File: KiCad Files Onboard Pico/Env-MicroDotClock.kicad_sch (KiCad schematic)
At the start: 60 parts, among them IC1 IS31FL3730-QFLS2-TR, IC2 IS31FL3730-QFLS2-TR, IC3 IS31FL3730-QFLS2-TR, IC4 IS31FL3730-QFLS2-TR, J1 Conn_01x06_Pin, J2 GT-USB-7051, M1 Dip-14 Socket, M2 Dip-14 Socket, M3 Dip-14 Socket, M4 Dip-14 Socket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

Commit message: Added onboard pico
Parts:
- removed J2: GT-USB-7051, Connector_USB:USB_C_Receptacle_G-Switch_GT-USB-7051x, symbol Connector:USB_C_Receptacle_USB2.0
- removed R13, R14: 5.1K 0805, Resistor_SMD:R_0805_2012Metric, symbol Device:R_Small
- removed SW1, SW2, SW3, SW4, SW5, SW6: SW_SPST, Button_Switch_SMD:SW_Push_SPST_NO_Alps_SKRK, symbol Switch:SW_SPST
- removed U1: Raspberry Pi Pico, MCU_RaspberryPi_and_Boards:RPi_Pico_SMD_TH, symbol MCU_RaspberryPi_and_Boards:Pico
- added SW1, SW2, SW3, SW4, SW5: SW_Push, Button_Switch_Keyboard:SW_Cherry_MX_1.00u_PCB, symbol Switch:SW_Push
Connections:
- net GND: now also SW1.2, SW2.2, SW3.2, SW4.2, SW5.2
- net GPIO2: now also SW1.1
- net GPIO3: now also SW2.1
- net GPIO4: now also SW3.1
- net GPIO5: now also SW4.1
- net GPIO6: now also SW5.1
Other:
- added sheet Onboard Pico (untitled.kicad_sch)

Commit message: for cat
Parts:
- added U1: Si7021-A20, Package_DFN_QFN:DFN-6-1EP_3x3mm_P1mm_EP1.5x2.4mm, symbol Sensor_Humidity:Si7021-A20
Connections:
- net I2C2_SCL is gone; now on net GPIO5: IC2.2 (SCL), R12.2
- net I2C2_SDA is gone; now on net GPIO4: IC2.1 (SDA), R11.2
- net I2C3_SCL is gone; now on net GPIO9: IC3.2 (SCL), R8.2
- net I2C3_SDA is gone; now on net GPIO8: IC3.1 (SDA), IC3.6 (AD), R7.2
- net RTC_SCL is gone; now on net GPIO7: R1.2, U3.16 (SCL)
- net RTC_SDA is gone; now on net GPIO6: R2.2, U3.15 (SDA)
- net +3V3: now also U1.5 (VDD)
- net GND: now also U1.2 (GND)
- net GPIO2: now also U1.1 (SDA)
- net GPIO3: now also U1.6 (SCL)
- net I2C1_SCL renamed GPIO1
- net I2C1_SDA renamed GPIO0
- net I2C4_SCL renamed GPIO13
- net I2C4_SDA renamed GPIO12
- no-connect marks 0 -> 1
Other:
- moved on the sheet: R7, R8

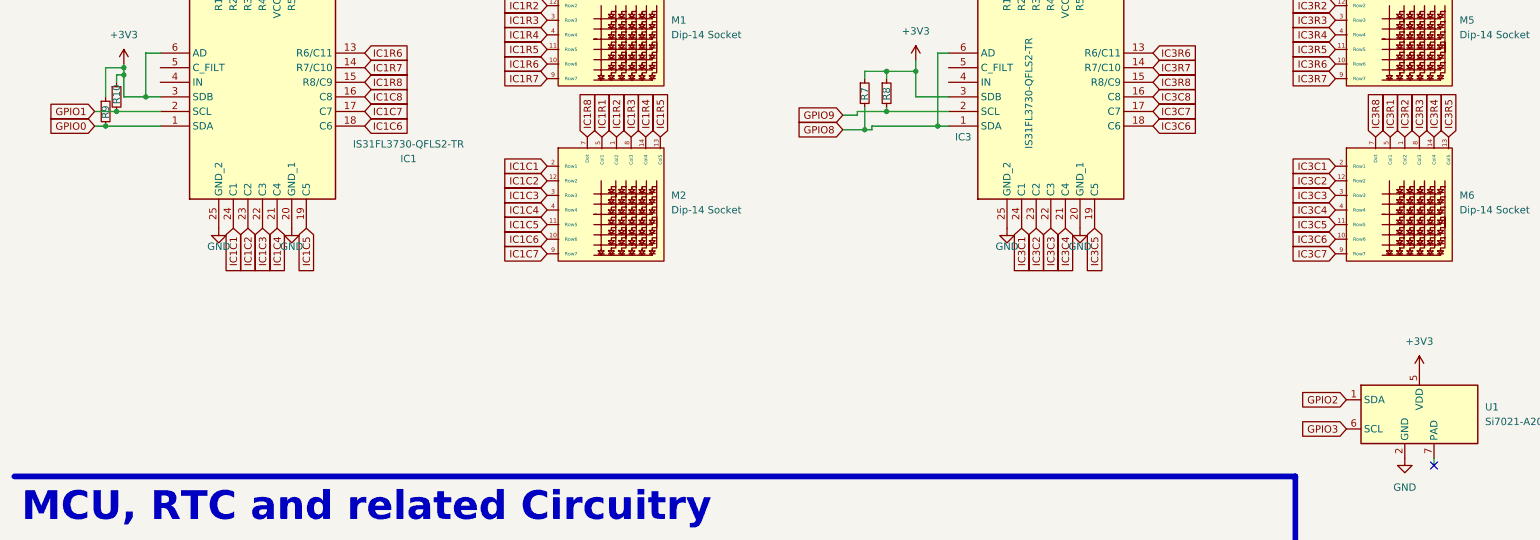
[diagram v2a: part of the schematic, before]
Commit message: Finished V1 Placement of onboard pico
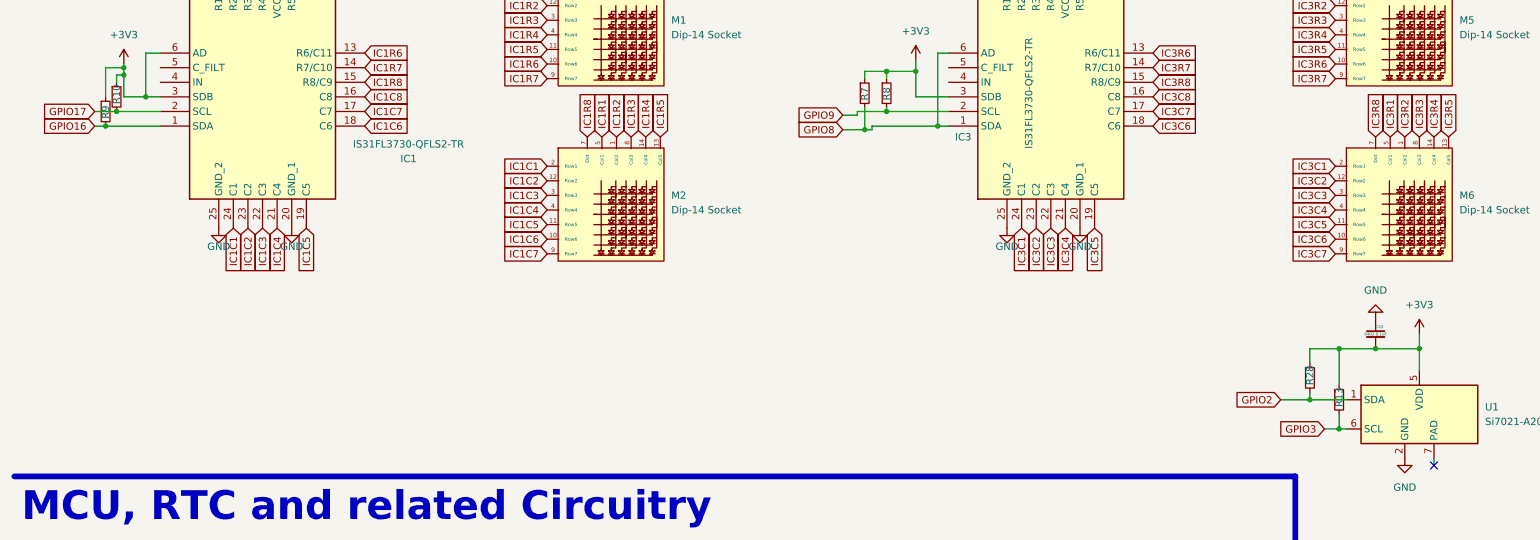
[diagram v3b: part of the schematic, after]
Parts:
- added C33: 0402 0.1uF, Capacitor_SMD:C_0402_1005Metric, symbol Device:C_Small
- added R13, R28: 0402 10K, Resistor_SMD:R_0402_1005Metric, symbol Device:R_Small
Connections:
- net +3V3: now also C33.2, R13.1, R28.1
- net GND: now also C33.1
- net GPIO2: now also R28.2
- net GPIO3: now also R13.2
- net GPIO0 renamed GPIO16
- net GPIO1 renamed GPIO17
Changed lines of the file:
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@@
   (junction (at 179.07 241.3) (diameter 0) (color 0 0 0 0)
   )
+  (junction (at 237.49 125.73) (diameter 0) (color 0 0 0 0)
+  )
   (junction (at 208.915 235.585) (diameter 0) (color 0 0 0 0)
   )
@@
   (junction (at 384.81 220.98) (diameter 0) (color 0 0 0 0)
   )
+  (junction (at 242.57 130.81) (diameter 0) (color 0 0 0 0)
+  )
   (junction (at 213.995 240.665) (diameter 0) (color 0 0 0 0)
   )
+  (junction (at 256.54 116.84) (diameter 0) (color 0 0 0 0)
+  )
   (junction (at 27.94 78.105) (diameter 0) (color 0 0 0 0)
   )
@@
   (junction (at 160.02 78.74) (diameter 0) (color 0 0 0 0)
   )
+  (junction (at 242.57 116.84) (diameter 0) (color 0 0 0 0)
+  )
   (junction (at 34.925 73.025) (diameter 0) (color 0 0 0 0)
   )
@@
   (junction (at 288.925 152.4) (diameter 0) (color 0 0 0 0)
   )
+  (junction (at 248.92 116.84) (diameter 0) (color 0 0 0 0)
+  )
   (junction (at 283.21 215.9) (diameter 0) (color 0 0 0 0)
   )
@@
     (stroke (width 0) (type default))
   )
+  (wire (pts (xy 256.54 116.84) (xy 256.54 120.65))
+    (stroke (width 0) (type default))
+  )
   (wire (pts (xy 160.02 78.74) (xy 161.29 78.74))
     (stroke (width 0) (type default))
@@
     (stroke (width 0) (type default))
   )
+  (wire (pts (xy 237.49 116.84) (xy 237.49 119.38))
+    (stroke (width 0) (type default))
+  )
   (wire (pts (xy 22.225 196.85) (xy 25.4 196.85))
     (stroke (width 0) (type default))
@@
     (stroke (width 0) (type default))
   )
+  (wire (pts (xy 240.03 130.81) (xy 242.57 130.81))
+    (stroke (width 0) (type default))
+  )
   (wire (pts (xy 290.83 144.78) (xy 290.83 142.875))
     (stroke (width 0) (type default))
@@
     (stroke (width 0) (type default))
   )
+  (wire (pts (xy 237.49 116.84) (xy 242.57 116.84))
+    (stroke (width 0) (type default))
+  )
   (wire (pts (xy 34.925 65.405) (xy 34.925 73.025))
     (stroke (width 0) (type default))
@@
     (stroke (width 0) (type default))
   )
+  (wire (pts (xy 237.49 125.73) (xy 243.84 125.73))
+    (stroke (width 0) (type default))
+  )
   (wire (pts (xy 205.74 217.805) (xy 205.74 215.265))
     (stroke (width 0) (type default))
@@
     (stroke (width 0) (type default))
   )
+  (wire (pts (xy 242.57 116.84) (xy 248.92 116.84))
+    (stroke (width 0) (type default))
+  )
+  (wire (pts (xy 237.49 124.46) (xy 237.49 125.73))
+    (stroke (width 0) (type default))
+  )
   (wire (pts (xy 276.86 215.9) (xy 283.21 215.9))
     (stroke (width 0) (type default))
   )
+  (wire (pts (xy 242.57 128.27) (xy 242.57 130.81))
+    (stroke (width 0) (type default))
+  )
   (wire (pts (xy 259.08 137.16) (xy 259.08 135.89))
     (stroke (width 0) (type default))
@@
     (stroke (width 1) (type default))
   )
+  (wire (pts (xy 232.41 125.73) (xy 237.49 125.73))
+    (stroke (width 0) (type default))
+  )
+  (wire (pts (xy 242.57 116.84) (xy 242.57 123.19))
+    (stroke (width 0) (type default))
+  )
   (wire (pts (xy 163.83 75.565) (xy 174.625 75.565))
     (stroke (width 0) (type default))
@@
     (stroke (width 0) (type default))
   )
+  (wire (pts (xy 248.92 116.84) (xy 256.54 116.84))
+    (stroke (width 0) (type default))
+  )
   (wire (pts (xy 163.83 74.93) (xy 163.83 75.565))
     (stroke (width 0) (type default))
@@
     (stroke (width 0) (type default))
   )
+  (wire (pts (xy 242.57 130.81) (xy 243.84 130.81))
+    (stroke (width 0) (type default))
+  )
   (wire (pts (xy 33.02 187.325) (xy 36.195 187.325))
     (stroke (width 0) (type default))
   )
+  (wire (pts (xy 256.54 114.3) (xy 256.54 116.84))
+    (stroke (width 0) (type default))
+  )
   (text_box "RTC and batery"
     (at 184.785 201.93 0) (size 60.96 45.72)
@@
     )
   )
-  (global_label "GPIO0" (shape input) (at 26.035 78.105 180) (fields_autoplaced)
+  (global_label "GPIO16" (shape input) (at 26.035 78.105 180) (fields_autoplaced)
     (effects (font (size 1.27 1.27)) (justify right))
-    (property "Intersheetrefs" "${INTERSHEET_REFS}" (at 17.365 78.105 0)
+    (property "Intersheetrefs" "${INTERSHEET_REFS}" (at 16.1555 78.105 0)
       (effects (font (size 1.27 1.27)) (justify right) hide)
     )
@@
     )
   )
-  (global_label "GPIO3" (shape input) (at 243.84 130.81 180) (fields_autoplaced)
+  (global_label "GPIO3" (shape input) (at 240.03 130.81 180) (fields_autoplaced)
     (effects (font (size 1.27 1.27)) (justify right))
-    (property "Intersheetrefs" "${INTERSHEET_REFS}" (at 235.17 130.81 0)
+    (property "Intersheetrefs" "${INTERSHEET_REFS}" (at 231.36 130.81 0)
       (effects (font (size 1.27 1.27)) (justify right) hide)
     )
@@
     )
   )
-  (global_label "GPIO1" (shape input) (at 26.035 75.565 180) (fields_autoplaced)
+  (global_label "GPIO17" (shape input) (at 26.035 75.565 180) (fields_autoplaced)
     (effects (font (size 1.27 1.27)) (justify right))
-    (property "Intersheetrefs" "${INTERSHEET_REFS}" (at 17.365 75.565 0)
+    (property "Intersheetrefs" "${INTERSHEET_REFS}" (at 16.1555 75.565 0)
       (effects (font (size 1.27 1.27)) (justify right) hide)
     )
@@
     )
   )
-  (global_label "GPIO2" (shape input) (at 243.84 125.73 180) (fields_autoplaced)
+  (global_label "GPIO2" (shape input) (at 232.41 125.73 180) (fields_autoplaced)
     (effects (font (size 1.27 1.27)) (justify right))
-    (property "Intersheetrefs" "${INTERSHEET_REFS}" (at 235.17 125.73 0)
+    (property "Intersheetrefs" "${INTERSHEET_REFS}" (at 223.74 125.73 0)
       (effects (font (size 1.27 1.27)) (justify right) hide)
     )
@@
     )
   )
+  (symbol (lib_id "Device:C_Small") (at 248.92 114.3 0) (unit 1)
+    (in_bom yes) (on_board yes) (dnp no)
+    (property "Reference" "C33" (at 249.555 113.03 0)
+      (effects (font (size 0.5 0.5)))
+    )
+    (property "Value" "0402 0.1uF" (at 248.92 114.3 0)
+      (effects (font (size 0.5 0.5)))
+    )
+    (property "Footprint" "Capacitor_SMD:C_0402_1005Metric" (at 248.92 114.3 0)
+      (effects (font (size 1.27 1.27)) hide)
+    )
+    (property "Datasheet" "~" (at 248.92 114.3 0)
+      (effects (font (size 1.27 1.27)) hide)
+    )
+    (pin "1")
+    (pin "2")
+    (instances
+      (project "Env-MicroDotClock"
+        (path "/3dbeb8d8-208e-4f6d-8d30-b14372f68a4f"
+          (reference "C33") (unit 1)
+        )
+      )
+    )
+  )
   (symbol (lib_id "power:GND") (at 254 135.89 0) (unit 1)
     (in_bom yes) (on_board yes) (dnp no) (fields_autoplaced)
@@
     )
   )
+  (symbol (lib_id "Device:R_Small") (at 237.49 121.92 0) (unit 1)
+    (in_bom yes) (on_board yes) (dnp no)
+    (property "Reference" "R28" (at 237.49 123.19 90)
+      (effects (font (size 1.27 1.27)) (justify left))
+    )
+    (property "Value" "0402 10K" (at 240.03 123.19 0)
+      (effects (font (size 1.27 1.27)) (justify left) hide)
+    )
+    (property "Footprint" "Resistor_SMD:R_0402_1005Metric" (at 237.49 121.92 0)
+      (effects (font (size 1.27 1.27)) hide)
+    )
+    (property "Datasheet" "~" (at 237.49 121.92 0)
+      (effects (font (size 1.27 1.27)) hide)
+    )
+    (pin "1")
+    (pin "2")
+    (instances
+      (project "Env-MicroDotClock"
+        (path "/3dbeb8d8-208e-4f6d-8d30-b14372f68a4f"
+          (reference "R28") (unit 1)
+        )
+      )
+    )
+  )
   (symbol (lib_id "Device:C_Small") (at 389.255 218.44 0) (unit 1)
     (in_bom yes) (on_board yes) (dnp no)
@@
     )
   )
+  (symbol (lib_id "Device:R_Small") (at 242.57 125.73 0) (unit 1)
+    (in_bom yes) (on_board yes) (dnp no)
+    (property "Reference" "R13" (at 242.57 127 90)
+      (effects (font (size 1.27 1.27)) (justify left))
+    )
+    (property "Value" "0402 10K" (at 245.11 127 0)
+      (effects (font (size 1.27 1.27)) (justify left) hide)
+    )
+    (property "Footprint" "Resistor_SMD:R_0402_1005Metric" (at 242.57 125.73 0)
+      (effects (font (size 1.27 1.27)) hide)
+    )
+    (property "Datasheet" "~" (at 242.57 125.73 0)
+      (effects (font (size 1.27 1.27)) hide)
+    )
+    (pin "1")
+    (pin "2")
+    (instances
+      (project "Env-MicroDotClock"
+        (path "/3dbeb8d8-208e-4f6d-8d30-b14372f68a4f"
+          (reference "R13") (unit 1)
+        )
+      )
+    )
+  )
   (symbol (lib_id "Switch:SW_Push") (at 173.99 241.3 0) (unit 1)
     (in_bom yes) (on_board yes) (dnp no) (fields_autoplaced)
@@
     )
   )
+  (symbol (lib_id "power:GND") (at 248.92 111.76 180) (unit 1)
+    (in_bom yes) (on_board yes) (dnp no) (fields_autoplaced)
+    (property "Reference" "#PWR029" (at 248.92 105.41 0)
+      (effects (font (size 1.27 1.27)) hide)
+    )
+    (property "Value" "GND" (at 248.92 106.68 0)
+      (effects (font (size 1.27 1.27)))
+    )
+    (property "Footprint" "" (at 248.92 111.76 0)
+      (effects (font (size 1.27 1.27)) hide)
+    )
+    (property "Datasheet" "" (at 248.92 111.76 0)
+      (effects (font (size 1.27 1.27)) hide)
+    )
+    (pin "1")
+    (instances
+      (project "Env-MicroDotClock"
+        (path "/3dbeb8d8-208e-4f6d-8d30-b14372f68a4f"
+          (reference "#PWR029") (unit 1)
+        )
+      )
+    )
+  )
   (symbol (lib_id "power:VCC") (at 321.31 124.46 0) (unit 1)
     (in_bom yes) (on_board yes) (dnp no) (fields_autoplaced)
@@
     )
   )
-  (symbol (lib_id "power:+3V3") (at 256.54 120.65 0) (unit 1)
+  (symbol (lib_id "power:+3V3") (at 256.54 114.3 0) (unit 1)
     (in_bom yes) (on_board yes) (dnp no) (fields_autoplaced)
-    (property "Reference" "#PWR027" (at 256.54 124.46 0)
+    (property "Reference" "#PWR027" (at 256.54 118.11 0)
       (effects (font (size 1.27 1.27)) hide)
     )
-    (property "Value" "+3V3" (at 256.54 115.57 0)
+    (property "Value" "+3V3" (at 256.54 109.22 0)
       (effects (font (size 1.27 1.27)))
     )
-    (property "Footprint" "" (at 256.54 120.65 0)
+    (property "Footprint" "" (at 256.54 114.3 0)
       (effects (font (size 1.27 1.27)) hide)
     )
-    (property "Datasheet" "" (at 256.54 120.65 0)
+    (property "Datasheet" "" (at 256.54 114.3 0)
       (effects (font (size 1.27 1.27)) hide)
     )

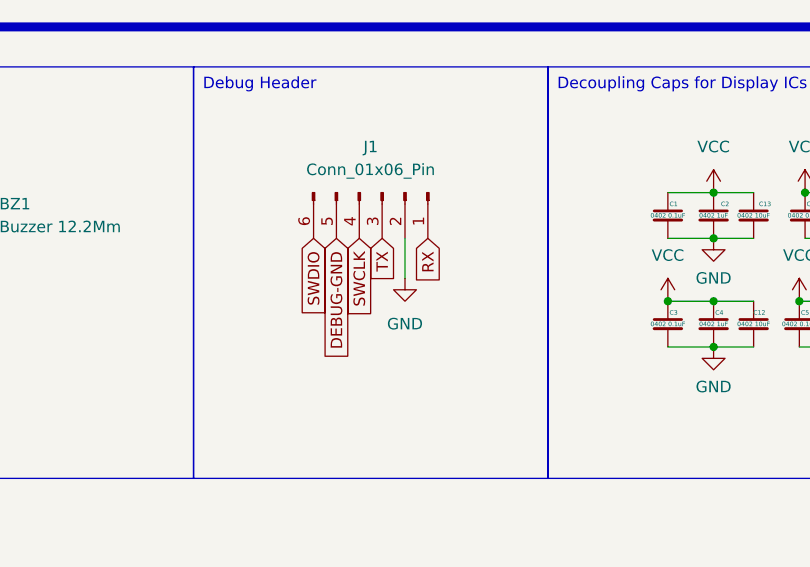
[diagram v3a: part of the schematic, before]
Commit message: Finished V2 placement and base wireing of RP2040
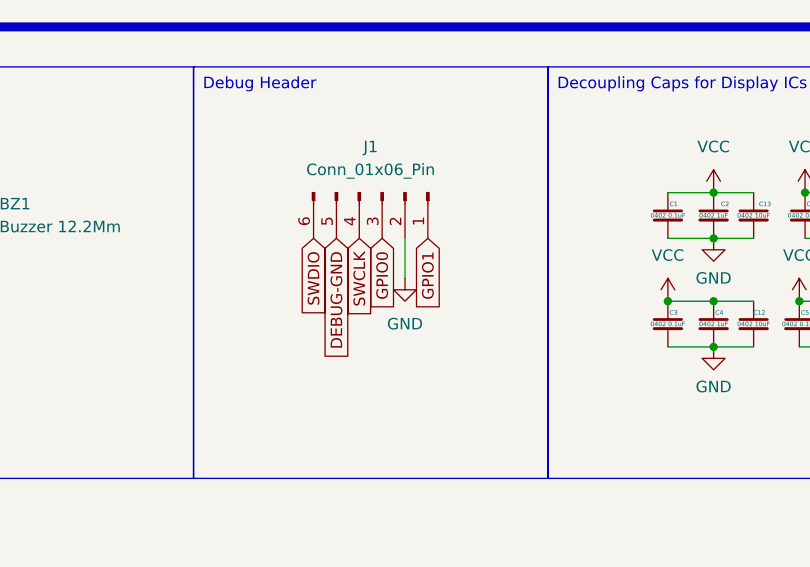
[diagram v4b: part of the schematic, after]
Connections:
- net RX renamed GPIO1
- net TX renamed GPIO0
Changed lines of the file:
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@@
     )
   )
-  (global_label "RX" (shape input) (at 337.82 220.98 270) (fields_autoplaced)
-    (effects (font (size 1.27 1.27)) (justify right))
-    (property "Intersheetrefs" "${INTERSHEET_REFS}" (at 337.82 226.4447 90)
+  (global_label "GPIO1" (shape input) (at 337.82 220.98 270) (fields_autoplaced)
+    (effects (font (size 1.27 1.27)) (justify right))
+    (property "Intersheetrefs" "${INTERSHEET_REFS}" (at 337.82 229.65 90)
       (effects (font (size 1.27 1.27)) (justify right) hide)
     )
@@
     )
   )
-  (global_label "TX" (shape input) (at 332.74 220.98 270) (fields_autoplaced)
-    (effects (font (size 1.27 1.27)) (justify right))
-    (property "Intersheetrefs" "${INTERSHEET_REFS}" (at 332.74 226.1423 90)
-      (effects (font (size 1.27 1.27)) (justify right) hide)
-    )
+  (global_label "GPIO0" (shape input) (at 332.74 220.98 270) (fields_autoplaced)
+    (effects (font (size 1.27 1.27)) (justify right))
+    (property "Intersheetrefs" "${INTERSHEET_REFS}" (at 332.74 229.65 90)
+      (effects (font (size 1.27 1.27)) (justify right) hide)
+    )
